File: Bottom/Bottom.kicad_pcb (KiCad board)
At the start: 2 copper layers, 40 x 40 mm, 42 parts, among them M1 Stepper_Motor_bipolar, M2 Stepper_Motor_bipolar, U1 GP2S60, U2 GP2S60, U7 DRV8833PWP, U8 DRV8833PWP

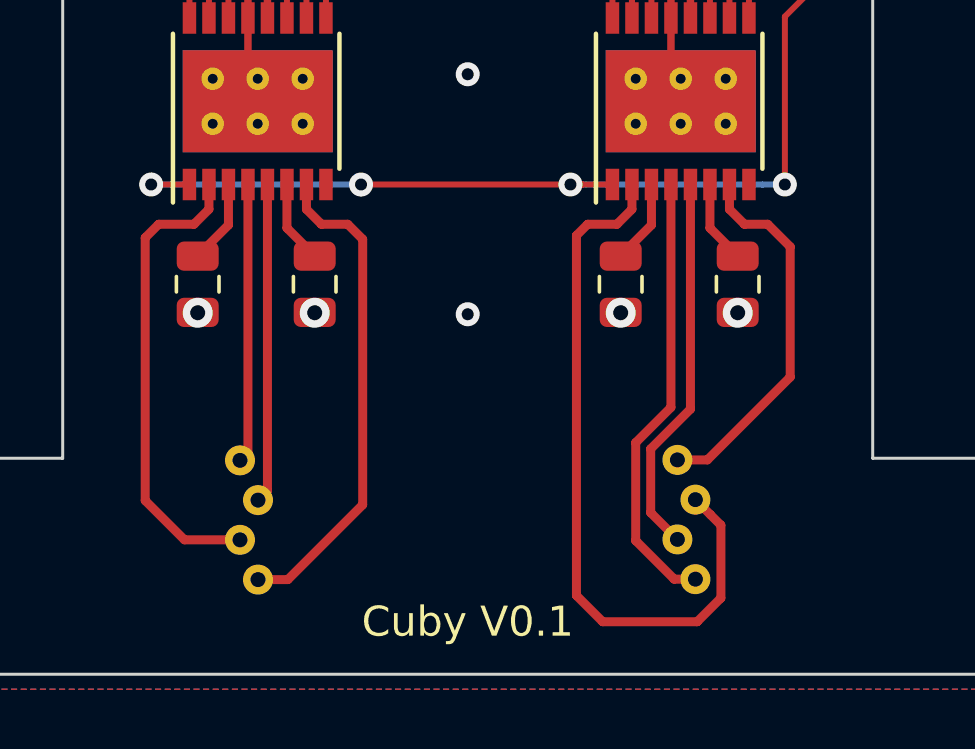
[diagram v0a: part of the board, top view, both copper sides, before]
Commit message: Changes to motor on bottom: fix mirrored pins
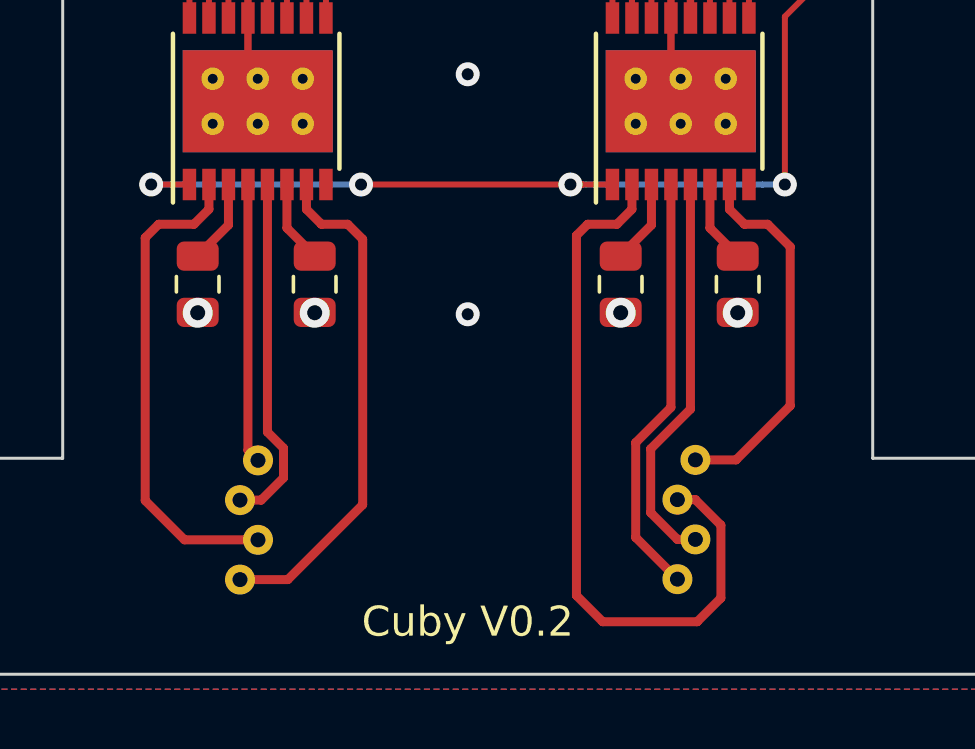
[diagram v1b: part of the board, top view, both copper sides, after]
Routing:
- net Net-(M1-Pad4): track 10.7 -> 11.8 mm
- net Net-(M2-Pad2): track 14.9 -> 14.2 mm
- net Net-(M2-Pad1): track 24.2 -> 24.8 mm
- net Net-(M2-Pad4): track 12.7 -> 13.3 mm
- net Net-(M1-Pad3): track 16.5 -> 17.1 mm
- net Net-(M1-Pad1): track 15.8 -> 16.4 mm
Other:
- board text added: "Cuby V0.2"
- board text removed: "Cuby V0.1"

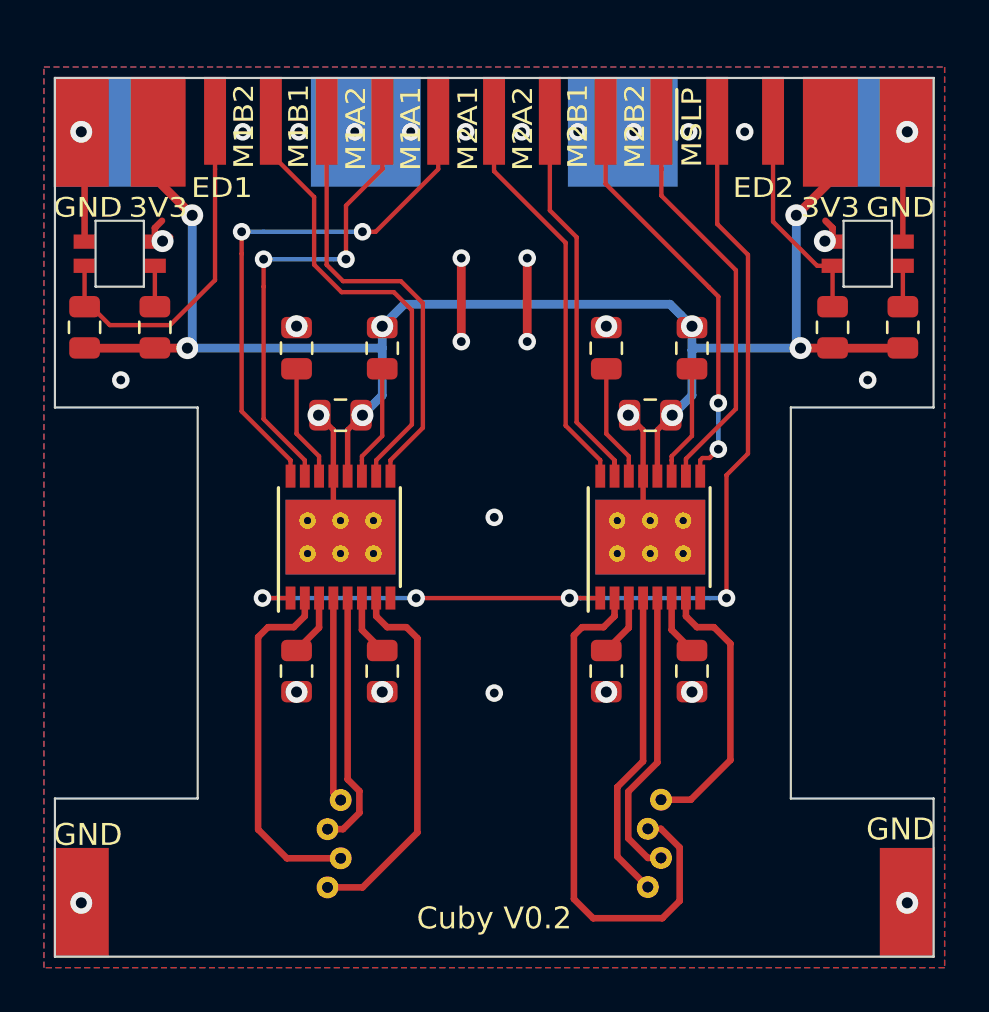
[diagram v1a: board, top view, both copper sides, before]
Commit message: updated bottom (motor placement, sharp sensor), front redesign, start op top redesign
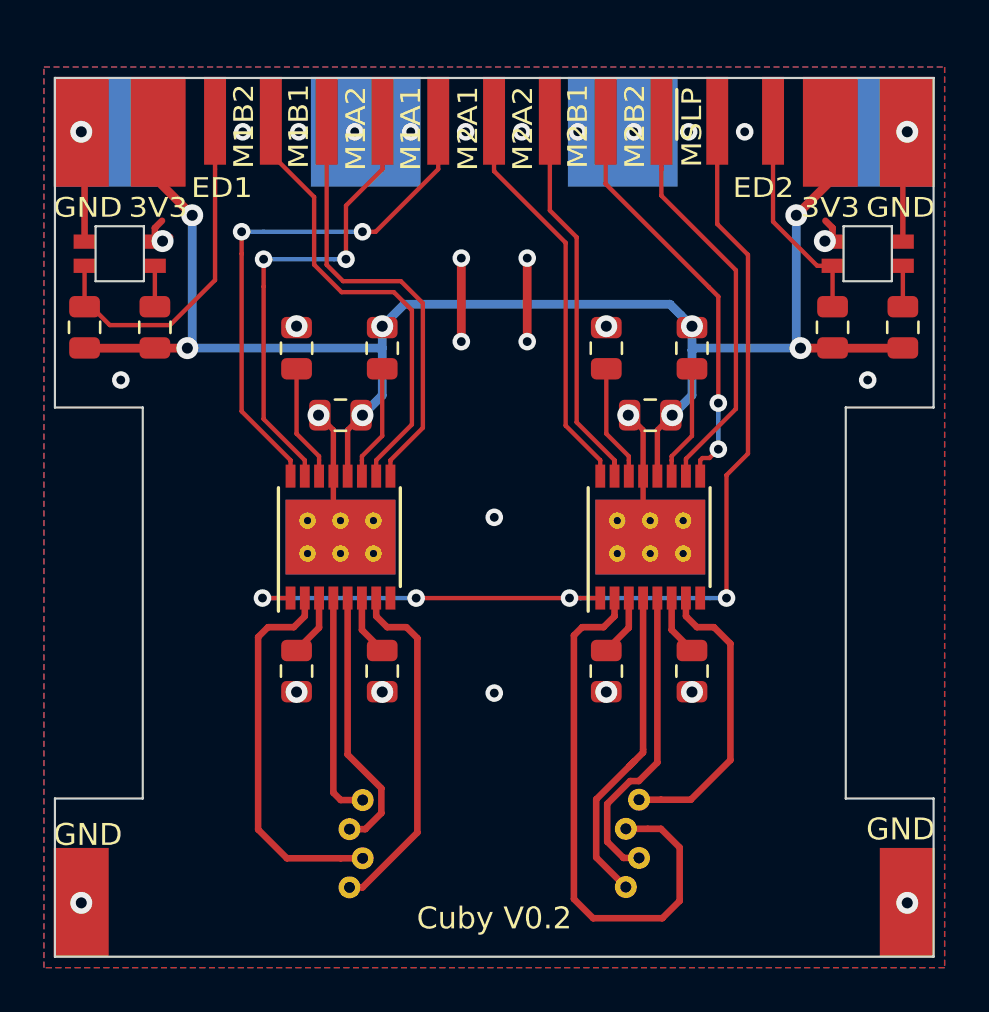
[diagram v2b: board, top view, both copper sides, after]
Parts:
- moved M1 1.00 mm to (166.7, 112.8)
- moved M2 1.00 mm to (179.3, 112.8)
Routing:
- net Net-(M2-Pad3): track 12.6 -> 13.6 mm
- net Net-(M2-Pad1): track 24.8 -> 25.8 mm
- net Net-(M1-Pad3): track 17.1 -> 16.1 mm
- net Net-(M1-Pad2): track 9.33 -> 10.3 mm
- net Net-(M1-Pad1): track 16.4 -> 17.4 mm
- net Net-(M2-Pad2): track 14.2 -> 14.9 mm
- net Net-(M2-Pad4): track 13.3 -> 14.0 mm
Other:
- outline, holes or cut-outs redrawn

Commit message: Update Top V0.2, small changes to motor placement
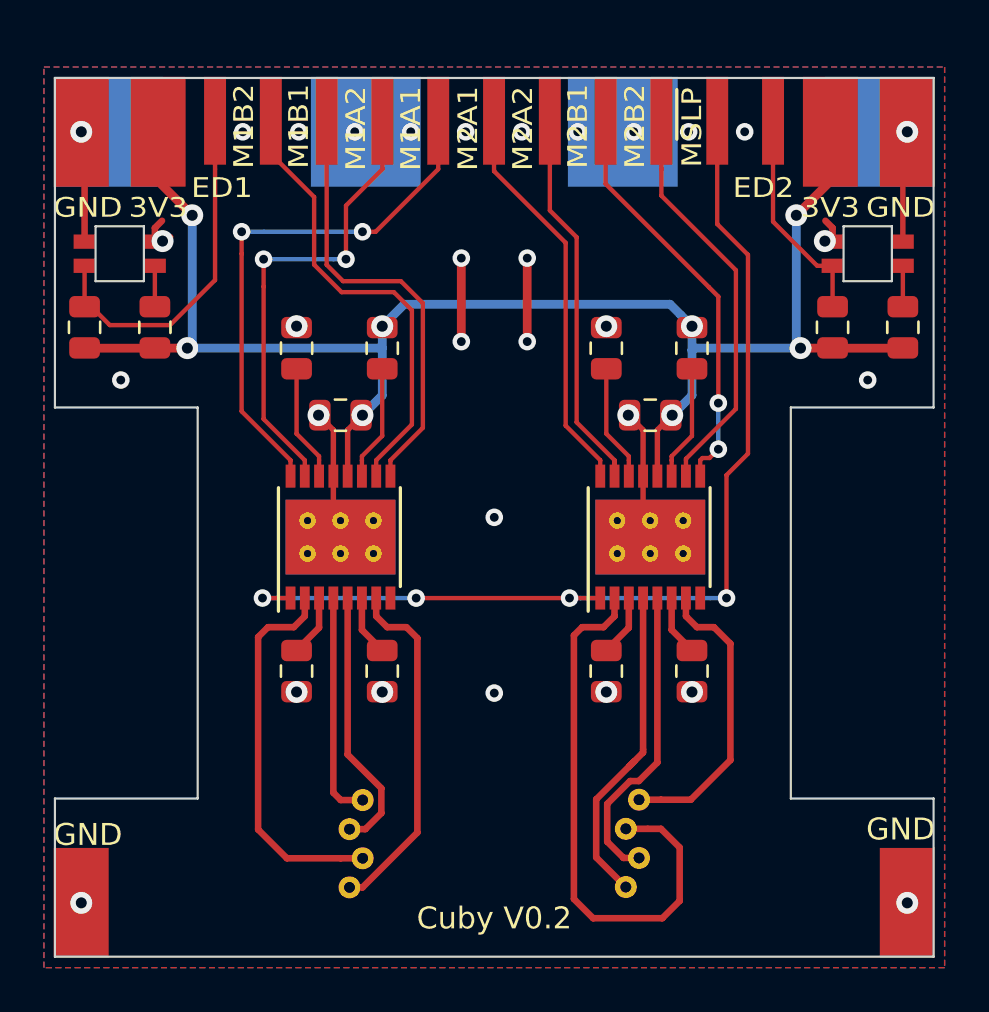
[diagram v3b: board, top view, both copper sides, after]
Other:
- outline, holes or cut-outs redrawn
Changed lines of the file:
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@@
     (visible_elements 7FFFFFFF)
     (pcbplotparams
-      (layerselection 0x010f0_ffffffff)
+      (layerselection 0x00030_7ffffffe)
       (usegerberextensions false)
       (usegerberattributes false)
@@
       (padsonsilk false)
       (subtractmaskfromsilk false)
-      (outputformat 1)
+      (outputformat 3)
       (mirror false)
       (drillshape 0)
@@
       (net 3 GND))
   )
+  (gr_line (start 153 93) (end 159.5 93) (layer Edge.Cuts) (width 0.1))
+  (gr_line (start 159.5 110.8) (end 153 110.8) (layer Edge.Cuts) (width 0.1))
+  (gr_line (start 159.5 110.8) (end 159.5 93) (layer Edge.Cuts) (width 0.1))
+  (gr_line (start 186.5 93) (end 193 93) (layer Edge.Cuts) (width 0.1))
+  (gr_line (start 186.5 110.8) (end 193 110.8) (layer Edge.Cuts) (width 0.1))
+  (gr_line (start 186.5 110.8) (end 186.5 93) (layer Edge.Cuts) (width 0.1))
   (gr_line (start 188.9 84.75) (end 188.9 87.25) (layer Edge.Cuts) (width 0.1))
   (gr_line (start 191.1 84.75) (end 191.1 87.25) (layer Edge.Cuts) (width 0.1))
@@
   (gr_line (start 154.85 84.75) (end 157.05 84.75) (layer Edge.Cuts) (width 0.1))
   (gr_line (start 157.05 87.25) (end 154.85 87.25) (layer Edge.Cuts) (width 0.1))
-  (gr_line (start 153 93) (end 157 93) (layer Edge.Cuts) (width 0.1))
-  (gr_line (start 153 110.8) (end 157 110.8) (layer Edge.Cuts) (width 0.1))
-  (gr_line (start 157 110.8) (end 157 93) (layer Edge.Cuts) (width 0.1))
-  (gr_line (start 189 93) (end 193 93) (layer Edge.Cuts) (width 0.1))
-  (gr_line (start 189 110.8) (end 193 110.8) (layer Edge.Cuts) (width 0.1))
-  (gr_line (start 189 110.8) (end 189 93) (layer Edge.Cuts) (width 0.1))
   (gr_text "Cuby V0.2" (at 173 116.25) (layer F.SilkS)
     (effects (font (size 1 1) (thickness 0.15)))

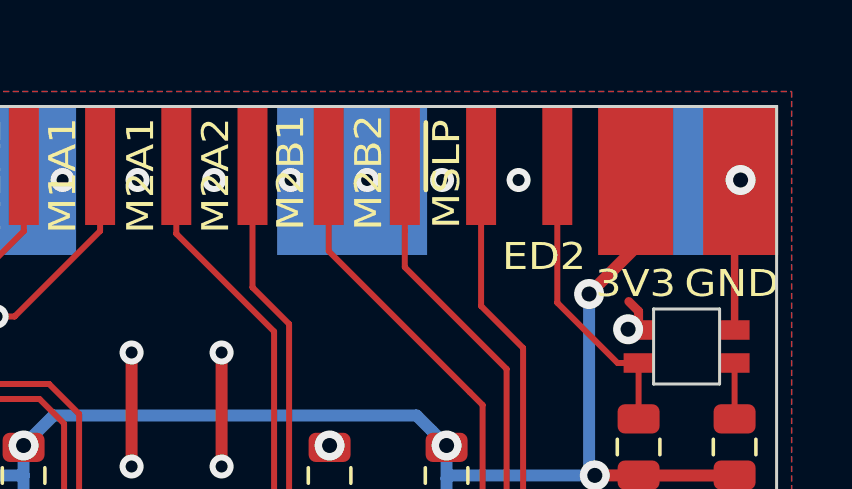
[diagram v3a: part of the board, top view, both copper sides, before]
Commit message: finish top, changes to front, added graphic
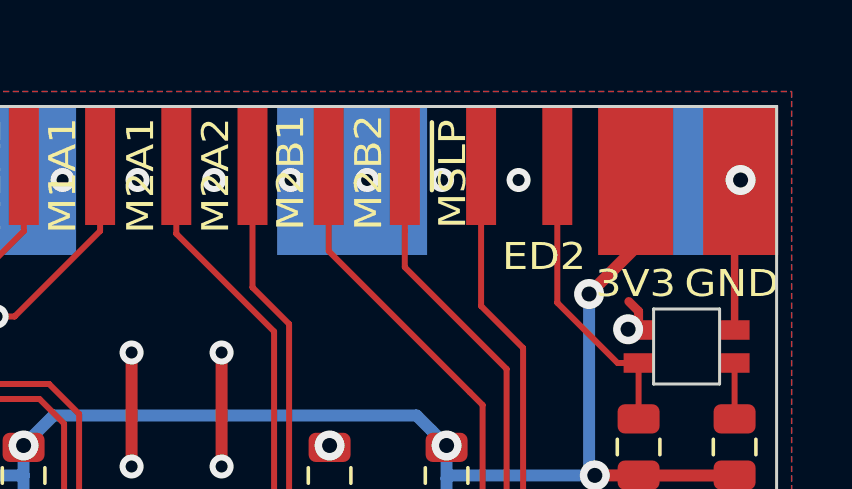
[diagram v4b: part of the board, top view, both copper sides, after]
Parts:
- removed G***: LOGO, Print:d2
- added G1: Graphic, Print:d2, B.Cu at (173.0, 98.0)

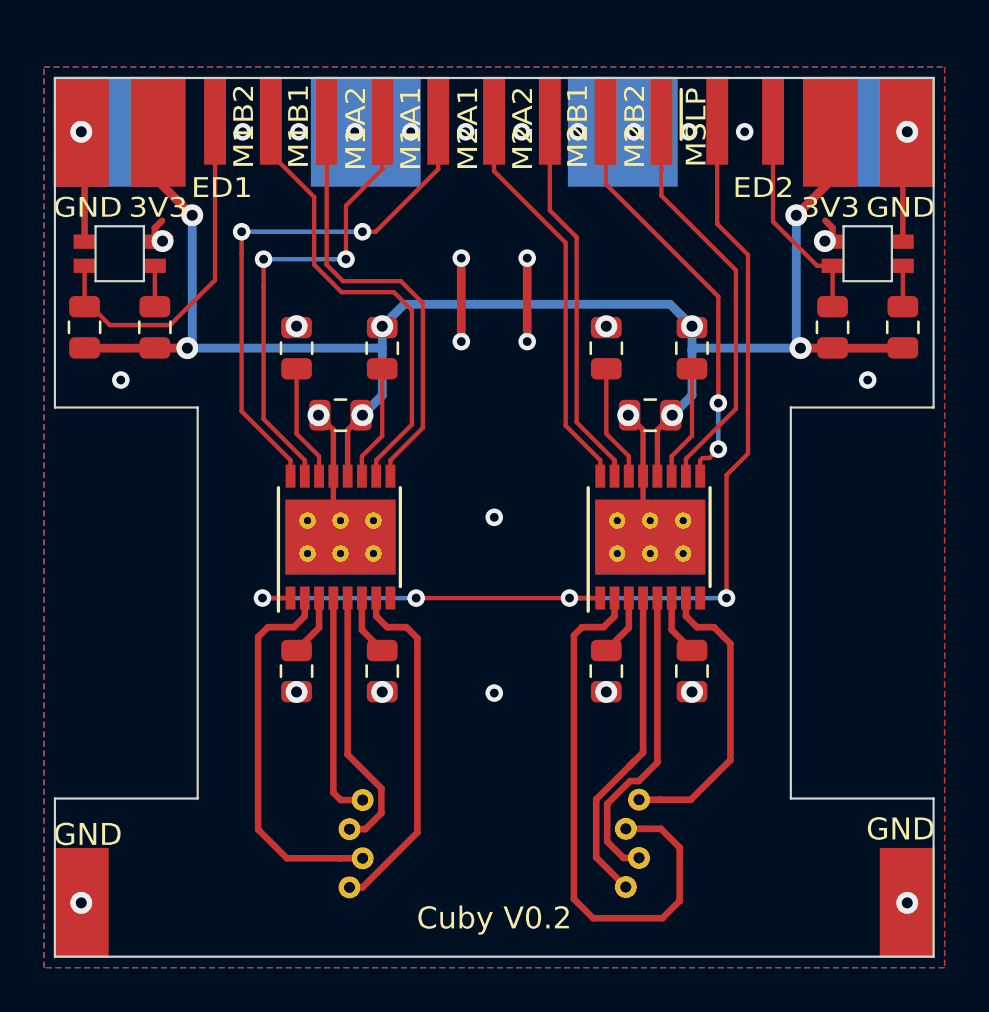
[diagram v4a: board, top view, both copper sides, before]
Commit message: Bottom, new motor, positioning and start routing
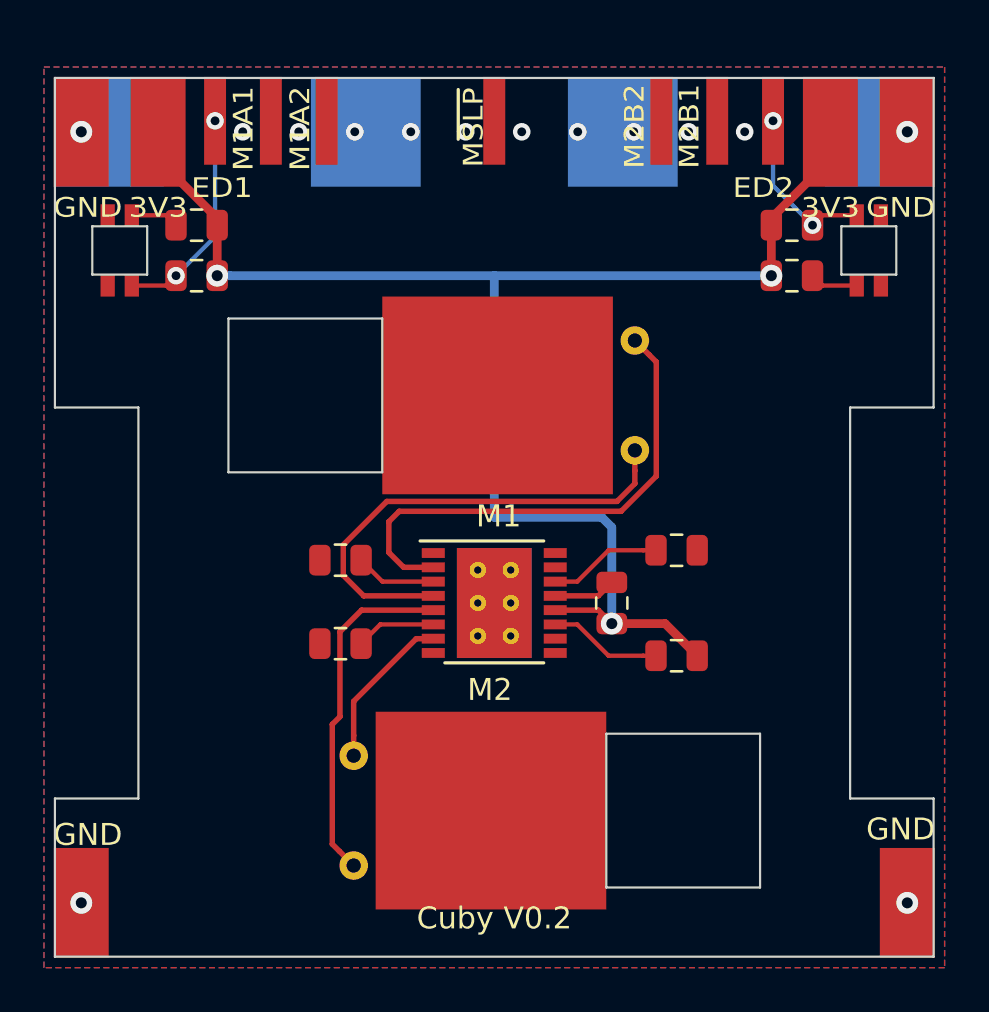
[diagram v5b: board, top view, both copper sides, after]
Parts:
- removed C11: 0.01µ, Capacitor_SMD:C_0805_2012Metric
- removed C12: 2.2µ, Capacitor_SMD:C_0805_2012Metric
- removed C13: 22µ, Capacitor_SMD:C_0805_2012Metric
- removed H10: M2B2, Custom:Mounting_Pad_Signal
- removed H7: M2A1, Custom:Mounting_Pad_Signal
- removed H8: M2A2, Custom:Mounting_Pad_Signal
- removed H9: M2B1, Custom:Mounting_Pad_Signal
- removed R13, R14: 1, Resistor_SMD:R_0805_2012Metric
- removed U8: DRV8833PWP, Package_SO:HTSSOP-16-1EP_4.4x5mm_P0.65mm_EP3.4x5mm_Mask2.46x2.31mm_ThermalVias
- H3: value M1B1 -> M2B1
- H4: value M1B2 -> M2B2
- M1, M2: value Stepper_Motor_bipolar -> Motor; footprint Custom:Medium_Stepper -> Custom:Small_DC_Motor
- moved M1 21.4 mm to (173.2, 92.5), turned to 0 degrees
- moved C9 19.6 mm to (181.3, 99.5), turned to 0 degrees
- moved C8 19.4 mm to (181.3, 104.3), turned to 180 degrees
- moved H3 17.8 mm to (183.2, 80.0)
- moved H4 17.8 mm to (180.6, 80.0)
- moved C10 15.0 mm to (178.3, 101.9), turned to 90 degrees
- moved H11 10.2 mm to (173.0, 80.0)
- moved H1 7.62 mm to (162.8, 80.0)
- moved U7 7.62 mm to (173.0, 101.9), turned to 0 degrees
- moved M2 6.62 mm to (172.8, 111.3), turned to 180 degrees
- moved R1 5.62 mm to (159.4, 87.0), turned to 180 degrees
- moved R4 5.57 mm to (186.6, 87.0), turned to 0 degrees
- moved R11 5.43 mm to (166.0, 100.0), turned to 180 degrees
- moved R2 5.02 mm to (159.4, 84.7), turned to 180 degrees
- moved R3 5.00 mm to (186.6, 84.7), turned to 0 degrees
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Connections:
- net /M1_~SLEEP renamed /M_~SLEEP
- H3 pad 1: /M1_BIN1 -> /M2_BIN1
- H4 pad 1: /M1_BIN2 -> /M2_BIN2
- M1 pad 1: Net-(M1-Pad1) -> (no net)
- M2 pad 1: Net-(M2-Pad1) -> (no net)
- U7 pad 10: /M1_BIN2 -> /M2_BIN2
- U7 pad 2: Net-(M1-Pad1) -> Net-(M1-Pad2)
- U7 pad 4: Net-(M1-Pad2) -> Net-(M1-Pad3)
- U7 pad 5: Net-(M1-Pad4) -> Net-(M2-Pad2)
- U7 pad 7: Net-(M1-Pad3) -> Net-(M2-Pad3)
- U7 pad 9: /M1_BIN1 -> /M2_BIN1
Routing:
- net /M_~SLEEP: track 46.6 -> 0.00 mm, vias 4 -> 0
- net GND: track 32.1 -> 2.83 mm, vias 32 -> 14
- net Net-(M2-Pad1): track 25.8 -> 0.00 mm
- net /M1_AIN1: track 24.4 -> 0.00 mm, vias 2 -> 0
- net /M1_BIN1: track 21.6 -> 0.00 mm
- net /M1_BIN2: track 20.9 -> 0.00 mm
- net /M1_AIN2: track 21.4 -> 1.50 mm, vias 2 -> 0
- net /M2_BIN1: track 19.2 -> 0.00 mm, vias 2 -> 0
- net /M2_BIN2: track 18.5 -> 0.00 mm
- net /M2_AIN1: track 18.5 -> 0.00 mm
- net /M2_AIN2: track 18.0 -> 0.00 mm
- net Net-(M1-Pad1): track 17.4 -> 0.00 mm
- net Net-(M2-Pad4): track 14.0 -> 0.00 mm
- net Net-(M1-Pad2): track 10.3 -> 23.3 mm
- net Net-(M1-Pad4): track 12.2 -> 0.00 mm
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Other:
- outline, holes or cut-outs redrawn

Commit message: finish bottom
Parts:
- moved C8 0.55 mm to (181.3, 103.8)
- moved C9 0.45 mm to (181.3, 100.0)
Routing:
- net /M1_AIN1: track 0.00 -> 38.2 mm
- net /M1_AIN2: track 1.50 -> 38.9 mm
- net /M2_BIN2: track 0.00 -> 34.1 mm
- net /M2_BIN1: track 0.00 -> 33.9 mm
- net /M_~SLEEP: track 0.00 -> 22.5 mm, vias 0 -> 2
- net GND: track 2.83 -> 9.47 mm, vias 14 -> 16
- net +3V3: track 70.3 -> 69.6 mm, vias 3 -> 4
